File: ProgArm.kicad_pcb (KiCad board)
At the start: 2 copper layers, 40 x 50 mm, 130 parts, among them M1 MOTOR, P1 I²C_Port, P10 TXD, P11 RING_VCC, P12 RING_GND, P13 RING_GPIOA_3_Port, P14 RING_GPIOA_4_Port, P15 RXD, P16 RING_BUTTONS_Port, P17 MicroUSB, P2 SPI_Port, P3 UART_Port, P4 SWD_Port, P5 GPIOA_1_2_Port, P6 TIM1_Port, P7 T_SENS, P8 RING_IR_OUT, P9 RING_LEDS_Port, Q1 MOS_P, Q2 MOS_P, Q3 MOS_P, Q4 MOS_P, Q5 MOS_P, Q6 MOS_P, Q7 MOS_P, Q8 MOS_P, SW1 FW/RST, SW2 ON/OFF, U1 TPS78330, U2 BQ24297, U3 LM3668, U4 STM32F103R, U5 MPU9250, U6 BQ27410, U7 SI1143, U8 LPS25H, U9 NRF8001, X1 32.768kHz, X2 8MHz, X3 16MHz

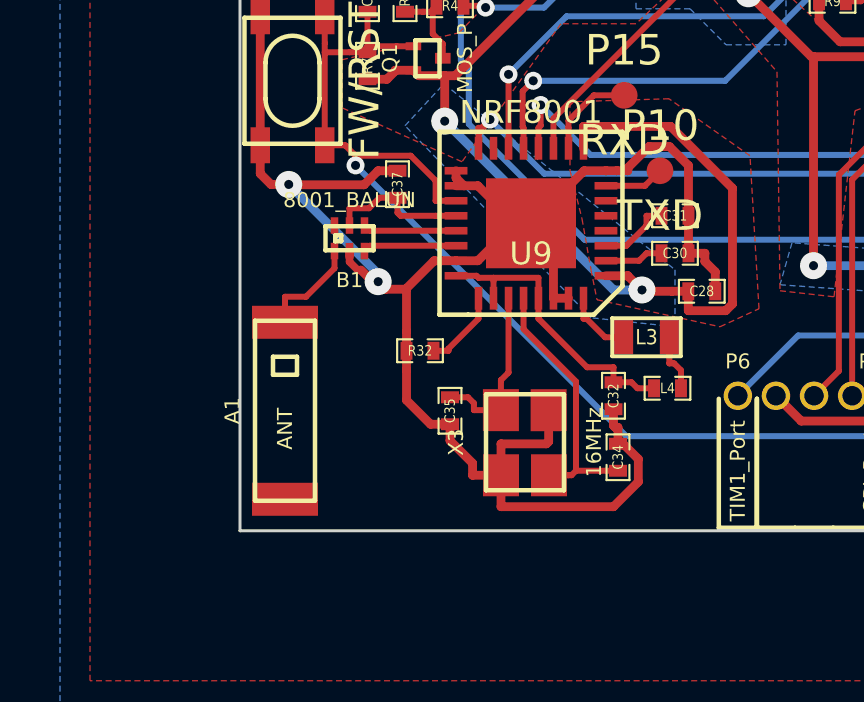
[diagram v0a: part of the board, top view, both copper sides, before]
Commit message: Made some changes to the antenna in accordance to app note
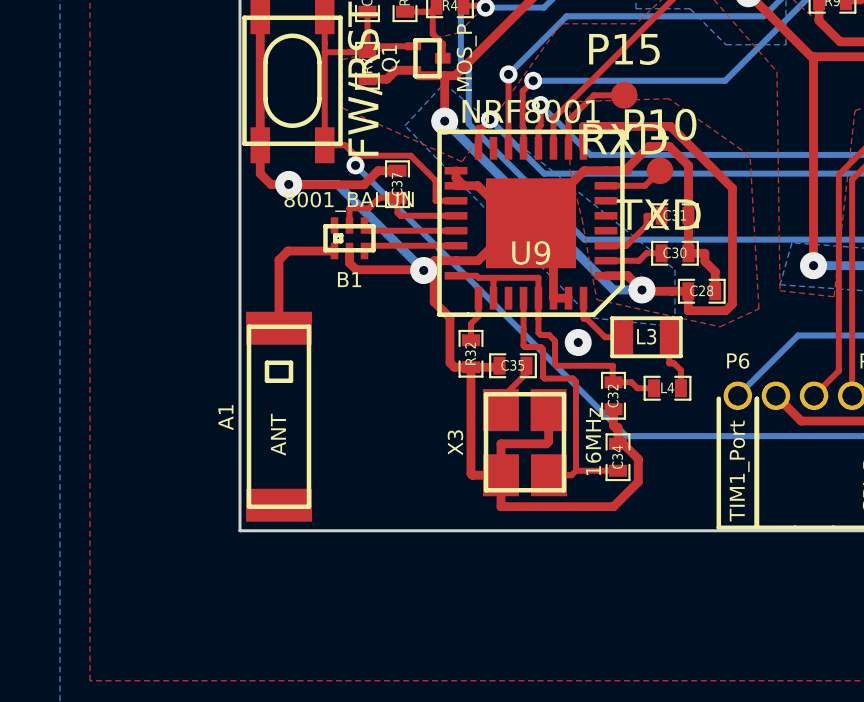
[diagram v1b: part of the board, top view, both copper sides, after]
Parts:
- moved C35 2.58 mm to (54.1, 89.5), turned to 180 degrees
- moved R32 1.70 mm to (52.7, 89.1), turned to 270 degrees
- moved A1 0.28 mm to (46.3, 91.2)
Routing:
- net N-00000119: track 5.85 -> 1.83 mm
- net GND: track 417.4 -> 419.8 mm, vias 9 -> 10
- net N-0000011: track 2.66 -> 1.50 mm
- net N-00000118: track 8.84 -> 9.70 mm
- net N-0000020: track 3.47 -> 4.25 mm
- net N-00000109: track 9.92 -> 10.7 mm

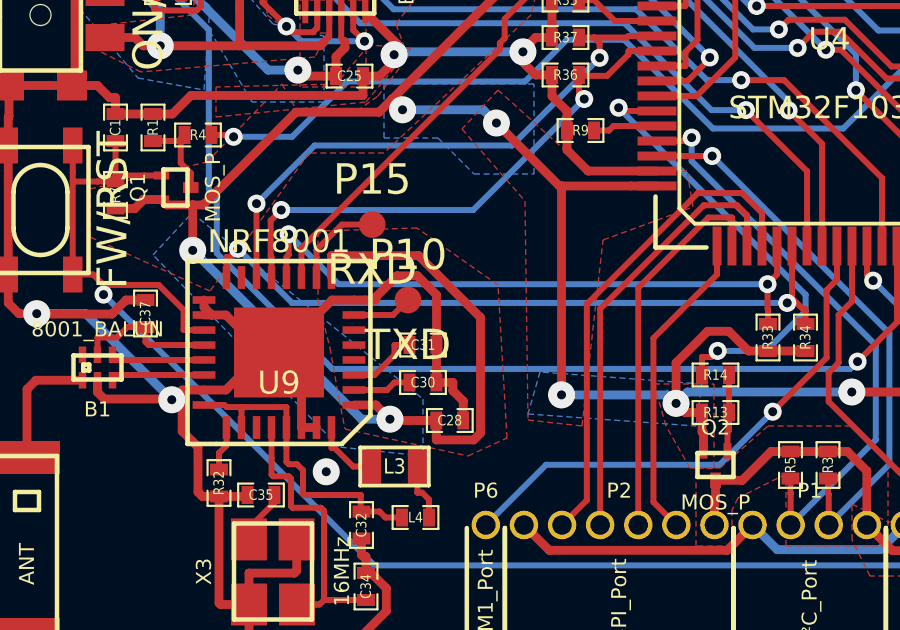
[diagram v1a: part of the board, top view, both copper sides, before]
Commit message: Better NRF central pad pour, wider GND pour near to it
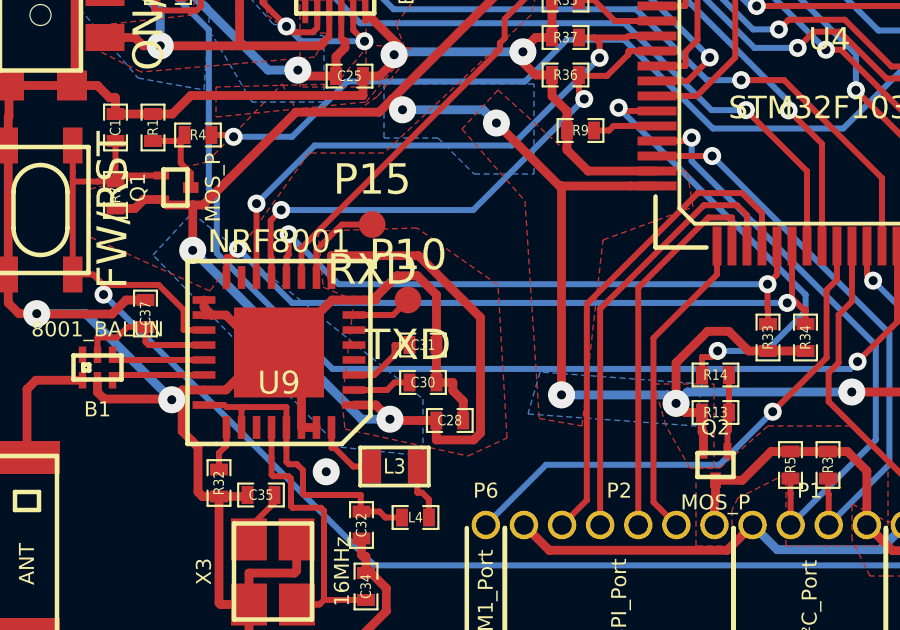
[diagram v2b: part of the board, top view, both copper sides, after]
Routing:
- net (no net): track 0.00 -> 0.12 mm, vias 0 -> 1
- net GND: track 419.8 -> 419.7 mm, vias 10 -> 9
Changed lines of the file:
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@@
-(kicad_pcb (version 3) (host pcbnew "(2013-07-07 BZR 4022)-stable")
+(kicad_pcb (version 3) (host pcbnew "(25-Oct-2014 BZR 4029)-stable")
   (general
     (links 365)
@@
   )
   (setup
-    (last_trace_width 0.295)
+    (last_trace_width 0.2)
     (user_trace_width 0.15)
     (user_trace_width 0.2)
@@
   (gr_line (start 85 45) (end 85 95) (angle 90) (layer Edge.Cuts) (width 0.1))
   (gr_line (start 45 45) (end 85 45) (angle 90) (layer Edge.Cuts) (width 0.1))
+  (segment (start 56.25 88.7) (end 56.275 88.725) (width 0.295) (layer F.Cu) (net 0))
+  (segment (start 56.3 88.75) (end 56.3 88.8) (width 0.295) (layer B.Cu) (net 0))
+  (segment (start 56.275 88.725) (end 56.3 88.75) (width 0.295) (layer B.Cu) (net 0))
+  (via (at 56.275 88.725) (size 0.9) (layers F.Cu B.Cu) (net 0))
   (via (at 67.9359 86.446) (size 0.9) (layers F.Cu B.Cu) (net 1))
   (via (at 51.8241 81.346) (size 0.9) (layers F.Cu B.Cu) (net 1))
@@
   (segment (start 54.2354 52.6562) (end 54.2354 55.4149) (width 0.2) (layer B.Cu) (net 26))
   (segment (start 54.0763 52.4971) (end 54.2354 52.6562) (width 0.2) (layer B.Cu) (net 26))
-  (segment (start 56.25 88.7) (end 56.275 88.725) (width 0.295) (layer F.Cu) (net 27))
-  (segment (start 56.3 88.75) (end 56.3 88.8) (width 0.295) (layer B.Cu) (net 27))
-  (segment (start 56.275 88.725) (end 56.3 88.75) (width 0.295) (layer B.Cu) (net 27))
-  (via (at 56.275 88.725) (size 0.9) (layers F.Cu B.Cu) (net 27))
   (segment (start 51.375 86.3) (end 51.15 86.3) (width 0.295) (layer F.Cu) (net 27))
   (via (at 46.6253 83.4555) (size 0.9) (layers F.Cu B.Cu) (net 27))
@@
   (segment (start 56.775 73.4) (end 56.775 74.275) (width 0.2) (layer F.Cu) (net 36))
   (segment (start 56.8793 74.3793) (end 56.8985 74.3985) (width 0.2) (layer F.Cu) (net 36))
-  (segment (start 57.425 89.5) (end 57.425 90.02542) (width 0.2) (layer F.Cu) (net 37) (status 800000))
+  (segment (start 57.425 89.5) (end 57.425 90.02542) (width 0.2) (layer F.Cu) (net 37))
   (segment (start 57.425 89.5) (end 55.55 89.5) (width 0.2) (layer F.Cu) (net 37))
   (segment (start 55.55 89.5) (end 55.5 89.45) (width 0.2) (layer F.Cu) (net 37))
@@
   (segment (start 54.9489 88.3989) (end 54.9489 87.9305) (width 0.2) (layer F.Cu) (net 37))
   (segment (start 55.024999 88.474999) (end 54.9489 88.3989) (width 0.2) (layer F.Cu) (net 37))
-  (segment (start 57.425 90.02542) (end 57.45 90.05042) (width 0.2) (layer F.Cu) (net 37) (status C00000))
+  (segment (start 57.425 90.02542) (end 57.45 90.05042) (width 0.2) (layer F.Cu) (net 37))
   (segment (start 57.45 90.0504) (end 58.0498 90.0504) (width 0.2) (layer F.Cu) (net 37))
   (segment (start 58.8004 90.25) (end 58.2494 90.25) (width 0.2) (layer F.Cu) (net 37))
@@
   (segment (start 49.3239 84.9989) (end 52.2006 84.9989) (width 0.2) (layer F.Cu) (net 44))
   (segment (start 49.15 84.825) (end 49.3239 84.9989) (width 0.2) (layer F.Cu) (net 44))
-  (segment (start 48.15 85.675) (end 46.6 85.675) (width 0.295) (layer F.Cu) (net 45) (status 400000))
-  (segment (start 46.3 85.975) (end 46.3 88.25) (width 0.295) (layer F.Cu) (net 45) (status 800000))
+  (segment (start 48.15 85.675) (end 46.6 85.675) (width 0.295) (layer F.Cu) (net 45))
+  (segment (start 46.3 85.975) (end 46.3 88.25) (width 0.295) (layer F.Cu) (net 45))
   (segment (start 46.6 85.675) (end 46.3 85.975) (width 0.295) (layer F.Cu) (net 45))
   (segment (start 51.4249 78.4348) (end 51.76 78.7699) (width 0.2) (layer F.Cu) (net 46))
@@
     (polygon
       (pts
-        (xy 62 76) (xy 60.8 77.3) (xy 62.9 79.7) (xy 63 87) (xy 64.8 87.2)
+        (xy 62 76) (xy 60.8 77.3) (xy 62.9 79.7) (xy 63.375 86.95) (xy 64.8 87.2)
         (xy 65.5 81) (xy 68.5 79.9) (xy 68.3 78.7) (xy 65 78.7)
       )
@@
     (polygon
       (pts
-        (xy 56.7 86.3) (xy 56.9 87.3) (xy 61 88.2) (xy 62.3 87.6) (xy 62 82.5)
-        (xy 59.3 80.6) (xy 56 80.7) (xy 56 83) (xy 56.4 84.6)
+        (xy 56.8 86.425) (xy 56.9 87.3) (xy 61 88.2) (xy 62.3 87.6) (xy 62 82.5)
+        (xy 59.3 80.6) (xy 56 80.7) (xy 56.175 82.575) (xy 57.2 83)
       )
     )

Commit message: Fixed GND VIA at nRF8001 chip
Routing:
- net GND: track 419.7 -> 421.4 mm, vias 9 -> 10
- net (no net): track 0.12 -> 0.00 mm, vias 1 -> 0
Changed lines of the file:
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@@
-(kicad_pcb (version 3) (host pcbnew "(25-Oct-2014 BZR 4029)-stable")
+(kicad_pcb (version 3) (host pcbnew "(2013-07-07 BZR 4022)-stable")
   (general
     (links 365)
@@
     (thickness 1.6)
     (drawings 4)
-    (tracks 1780)
+    (tracks 1781)
     (zones 0)
     (modules 130)
@@
   (gr_line (start 85 45) (end 85 95) (angle 90) (layer Edge.Cuts) (width 0.1))
   (gr_line (start 45 45) (end 85 45) (angle 90) (layer Edge.Cuts) (width 0.1))
-  (segment (start 56.25 88.7) (end 56.275 88.725) (width 0.295) (layer F.Cu) (net 0))
-  (segment (start 56.3 88.75) (end 56.3 88.8) (width 0.295) (layer B.Cu) (net 0))
-  (segment (start 56.275 88.725) (end 56.3 88.75) (width 0.295) (layer B.Cu) (net 0))
-  (via (at 56.275 88.725) (size 0.9) (layers F.Cu B.Cu) (net 0))
   (via (at 67.9359 86.446) (size 0.9) (layers F.Cu B.Cu) (net 1))
   (via (at 51.8241 81.346) (size 0.9) (layers F.Cu B.Cu) (net 1))
@@
   (segment (start 54.2354 52.6562) (end 54.2354 55.4149) (width 0.2) (layer B.Cu) (net 26))
   (segment (start 54.0763 52.4971) (end 54.2354 52.6562) (width 0.2) (layer B.Cu) (net 26))
+  (segment (start 55.94968 87.24936) (end 55.94968 88.39968) (width 0.295) (layer F.Cu) (net 27) (status 400000))
+  (segment (start 56.3 88.75) (end 56.3 88.775) (width 0.295) (layer B.Cu) (net 27))
+  (segment (start 56.275 88.725) (end 56.3 88.75) (width 0.295) (layer B.Cu) (net 27))
+  (via (at 56.275 88.725) (size 0.9) (layers F.Cu B.Cu) (net 27))
+  (segment (start 55.94968 88.39968) (end 56.275 88.725) (width 0.295) (layer F.Cu) (net 27))
   (segment (start 51.375 86.3) (end 51.15 86.3) (width 0.295) (layer F.Cu) (net 27))
   (via (at 46.6253 83.4555) (size 0.9) (layers F.Cu B.Cu) (net 27))

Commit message: Made minor changes to the ground plane
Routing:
- net GND: track 421.4 -> 423.2 mm, vias 10 -> 11
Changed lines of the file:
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@@
     (thickness 1.6)
     (drawings 4)
-    (tracks 1781)
+    (tracks 1784)
     (zones 0)
     (modules 130)
@@
   (layers
     (15 F.Cu signal)
-    (0 B.Cu signal)
+    (0 B.Cu signal hide)
     (16 B.Adhes user)
     (17 F.Adhes user)
@@
   (gr_line (start 85 45) (end 85 95) (angle 90) (layer Edge.Cuts) (width 0.1))
   (gr_line (start 45 45) (end 85 45) (angle 90) (layer Edge.Cuts) (width 0.1))
+  (via (at 60.7687 67.1277) (size 0.9) (layers F.Cu B.Cu) (net 1))
+  (segment (start 61.087 66.8094) (end 60.7687 67.1277) (width 0.295) (layer F.Cu) (net 1))
   (via (at 67.9359 86.446) (size 0.9) (layers F.Cu B.Cu) (net 1))
   (via (at 51.8241 81.346) (size 0.9) (layers F.Cu B.Cu) (net 1))
   (via (at 57.6245 64.5691) (size 0.9) (layers F.Cu B.Cu) (net 1))
   (via (at 73.7929 86.0669) (size 0.9) (layers F.Cu B.Cu) (net 1))
-  (via (at 60.7687 67.1277) (size 0.9) (layers F.Cu B.Cu) (net 1))
   (via (at 58.399 86.9733) (size 0.9) (layers F.Cu B.Cu) (net 1))
   (via (at 80.0289 54.946) (size 0.9) (layers F.Cu B.Cu) (net 1))
@@
   (segment (start 66.5039 56.4099) (end 67.7847 57.6907) (width 0.295) (layer B.Cu) (net 1))
   (segment (start 66.1357 56.4099) (end 66.5039 56.4099) (width 0.295) (layer B.Cu) (net 1))
-  (segment (start 61.087 66.8094) (end 60.7687 67.1277) (width 0.295) (layer F.Cu) (net 1))
   (segment (start 61.087 65.725) (end 61.087 66.8094) (width 0.295) (layer F.Cu) (net 1))
   (segment (start 77.3566 82.756) (end 76.799 82.1984) (width 0.295) (layer F.Cu) (net 1))
@@
   (segment (start 54.2354 52.6562) (end 54.2354 55.4149) (width 0.2) (layer B.Cu) (net 26))
   (segment (start 54.0763 52.4971) (end 54.2354 52.6562) (width 0.2) (layer B.Cu) (net 26))
-  (segment (start 55.94968 87.24936) (end 55.94968 88.39968) (width 0.295) (layer F.Cu) (net 27) (status 400000))
+  (segment (start 83.256 87.7867) (end 83.256 89.619) (width 0.295) (layer B.Cu) (net 27))
+  (via (at 83.25 89.625) (size 0.9) (layers F.Cu B.Cu) (net 27))
+  (segment (start 83.256 89.619) (end 83.25 89.625) (width 0.295) (layer B.Cu) (net 27))
+  (segment (start 55.94968 87.24936) (end 55.94968 88.39968) (width 0.295) (layer F.Cu) (net 27))
   (segment (start 56.3 88.75) (end 56.3 88.775) (width 0.295) (layer B.Cu) (net 27))
   (segment (start 56.275 88.725) (end 56.3 88.75) (width 0.295) (layer B.Cu) (net 27))
